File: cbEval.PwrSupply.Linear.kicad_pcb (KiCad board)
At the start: 2 copper layers, 35 x 109 mm, 38 parts, among them J1 CAL.CT3151V1-0, J10 Socket.Hor.2x5.6-5535512-4, J2 CAL.CT3151V1-2, J3 Keystone.4918, J4 Keystone.4918, J5 Keystone.3571, J6 Keystone.3571, J7 Socket.Hor.2x5.6-5535512-4, J8 Header.Hor.2x5.9-103326-0-05, J9 Header.Hor.2x5.9-103326-0-05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

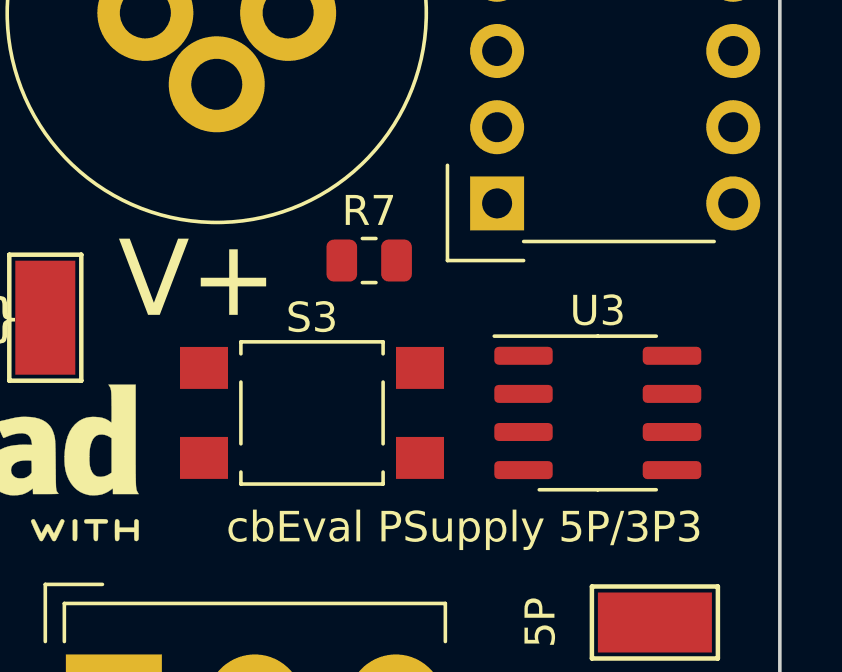
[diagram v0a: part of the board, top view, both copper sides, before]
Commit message: Bus-Leitungen neu belegt
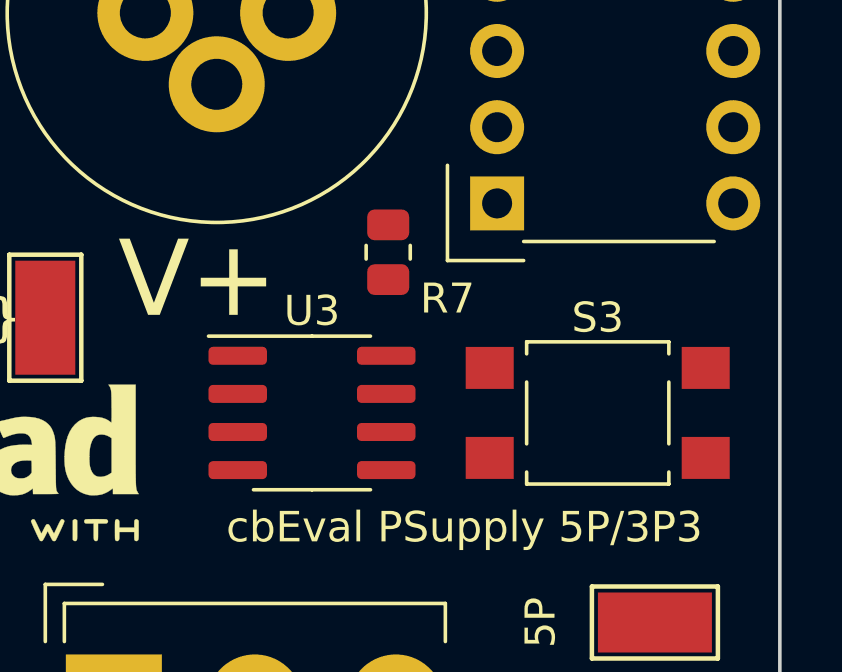
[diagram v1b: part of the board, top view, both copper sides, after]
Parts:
- moved S3 9.52 mm to (157.5, 77.5)
- moved U3 9.52 mm to (148.0, 77.5)
- moved R7 0.69 mm to (150.5, 72.1), turned to -90 degrees
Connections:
- J10 pad 10: /I2C-SCL -> /One-Wire
- J10 pad 9: /I2C-SDA -> /SPI-ADR2
- J7 pad 10: /PwrBus-Rsrvd1 -> /I2C-SCL
- J7 pad 9: /PwrBus-Rsrvd0 -> /I2C-SDA
- J8 pad 10: /PwrBus-Rsrvd1 -> /I2C-SCL
- J8 pad 9: /PwrBus-Rsrvd0 -> /I2C-SDA
- J9 pad 10: /I2C-SCL -> /One-Wire
- J9 pad 9: /I2C-SDA -> /SPI-ADR2
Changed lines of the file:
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@@
   (net 7 "Net-(D2-Pad4)")
   (net 8 "Net-(D1-Pad2)")
-  (net 9 "Net-(S2-Pad4)")
-  (net 10 "Net-(S2-Pad6)")
+  (net 9 "/SPI-ADR2")
+  (net 10 "/One-Wire")
   (net 11 "Net-(D2-Pad2)")
   (net 12 "+VDC")
@@
   (net 16 "unconnected-(S1-Pad4)")
   (net 17 "unconnected-(S1-Pad1)")
-  (net 18 "/PwrBus-Rsrvd1")
-  (net 19 "/PwrBus-Rsrvd0")
+  (net 18 "Net-(R5-Pad1)")
+  (net 19 "Net-(R6-Pad1)")
   (net 20 "~PWR-FAIL")
   (net 21 "-15V")
@@
       (net 5 "~RESET") (pinfunction "8") (pintype "passive"))
     (pad "9" thru_hole circle (at -7.87 -5.08) (size 1.8 1.8) (drill 1) (layers *.Cu *.Mask)
-      (net 19 "/PwrBus-Rsrvd0") (pinfunction "9") (pintype "passive"))
+      (net 24 "/I2C-SDA") (pinfunction "9") (pintype "passive"))
     (pad "10" thru_hole circle (at 0 -5.08) (size 1.8 1.8) (drill 1) (layers *.Cu *.Mask)
-      (net 18 "/PwrBus-Rsrvd1") (pinfunction "10") (pintype "passive"))
+      (net 23 "/I2C-SCL") (pinfunction "10") (pintype "passive"))
   )
   (footprint "BTech.Connector.4mm:CAL.CT3151V1" (layer "F.Cu")
@@
       (net 5 "~RESET") (pinfunction "8") (pintype "passive"))
     (pad "9" thru_hole oval (at 0 10.16 180) (locked) (size 1.7 1.7) (drill 1) (layers *.Cu *.Mask)
-      (net 19 "/PwrBus-Rsrvd0") (pinfunction "9") (pintype "passive"))
+      (net 24 "/I2C-SDA") (pinfunction "9") (pintype "passive"))
     (pad "10" thru_hole oval (at 2.54 10.16 180) (locked) (size 1.7 1.7) (drill 1) (layers *.Cu *.Mask)
-      (net 18 "/PwrBus-Rsrvd1") (pinfunction "10") (pintype "passive"))
+      (net 23 "/I2C-SCL") (pinfunction "10") (pintype "passive"))
     (model "${KICAD6_3DMODEL_DIR}/Connector_PinHeader_2.54mm.3dshapes/PinHeader_2x05_P2.54mm_Horizontal.wrl"
       (offset (xyz 0 0 0))
@@
     (fp_line (start 1 -0.625) (end 1 0.625) (layer "F.Fab") (width 0.1))
     (pad "1" smd roundrect (at -0.9125 0 90) (locked) (size 1.025 1.4) (layers "F.Cu" "F.Paste" "F.Mask") (roundrect_rratio 0.243902)
-      (net 8 "Net-(D1-Pad2)"))
+      (net 8 "Net-(D1-Pad2)") (pintype "passive"))
     (pad "2" smd roundrect (at 0.9125 0 90) (locked) (size 1.025 1.4) (layers "F.Cu" "F.Paste" "F.Mask") (roundrect_rratio 0.243902)
-      (net 3 "+5V"))
+      (net 3 "+5V") (pintype "passive"))
     (model "${KICAD6_3DMODEL_DIR}/Resistor_SMD.3dshapes/R_0805_2012Metric.wrl"
       (offset (xyz 0 0 0))
@@
       (net 4 "+3V3") (pinfunction "C") (pintype "passive"))
     (pad "4" thru_hole circle (at -4.7 2.415) (size 3.2 3.2) (drill 1.9) (layers *.Cu *.Mask)
-      (net 9 "Net-(S2-Pad4)") (pinfunction "A") (pintype "passive"))
+      (net 18 "Net-(R5-Pad1)") (pinfunction "A") (pintype "passive"))
     (pad "5" thru_hole circle (at 0 2.415) (size 3.2 3.2) (drill 1.9) (layers *.Cu *.Mask)
       (net 3 "+5V") (pinfunction "B") (pintype "passive"))
     (pad "6" thru_hole circle (at 4.7 2.415) (size 3.2 3.2) (drill 1.9) (layers *.Cu *.Mask)
-      (net 10 "Net-(S2-Pad6)") (pinfunction "C") (pintype "passive"))
+      (net 19 "Net-(R6-Pad1)") (pinfunction "C") (pintype "passive"))
   )
   (footprint "BTech.Connector.QuickConnect:Keystone.4918" (layer "F.Cu")
@@
     (fp_line (start 1 -0.625) (end 1 0.625) (layer "F.Fab") (width 0.1))
     (pad "1" smd roundrect (at -0.9125 0 270) (locked) (size 1.025 1.4) (layers "F.Cu" "F.Paste" "F.Mask") (roundrect_rratio 0.243902)
-      (net 10 "Net-(S2-Pad6)") (pintype "passive"))
+      (net 19 "Net-(R6-Pad1)") (pintype "passive"))
     (pad "2" smd roundrect (at 0.9125 0 270) (locked) (size 1.025 1.4) (layers "F.Cu" "F.Paste" "F.Mask") (roundrect_rratio 0.243902)
       (net 7 "Net-(D2-Pad4)") (pintype "passive"))
@@
   )
   (footprint "Package_SO:SOIC-8_3.9x4.9mm_P1.27mm" (layer "F.Cu")
-    (at 157.48 77.47)
+    (at 147.955 77.47)
     (descr "SOIC, 8 Pin (JEDEC MS-012AA, https://www.analog.com/media/en/package-pcb-resources/package/pkg_pdf/soic_narrow-r/r_8.pdf), generated with kicad-footprint-generator ipc_gullwing_generator.py")
     (tags "SOIC SO")
@@
       (net 25 "/SPI-ADR1") (pinfunction "8") (pintype "passive"))
     (pad "9" thru_hole oval (at 0 10.16 180) (locked) (size 1.7 1.7) (drill 1) (layers *.Cu *.Mask)
-      (net 24 "/I2C-SDA") (pinfunction "9") (pintype "passive"))
+      (net 9 "/SPI-ADR2") (pinfunction "9") (pintype "passive"))
     (pad "10" thru_hole oval (at 2.54 10.16 180) (locked) (size 1.7 1.7) (drill 1) (layers *.Cu *.Mask)
-      (net 23 "/I2C-SCL") (pinfunction "10") (pintype "passive"))
+      (net 10 "/One-Wire") (pinfunction "10") (pintype "passive"))
     (model "${KICAD6_3DMODEL_DIR}/Connector_PinHeader_2.54mm.3dshapes/PinHeader_2x05_P2.54mm_Horizontal.wrl"
       (offset (xyz 0 0 0))
@@
   )
   (footprint "Button_Switch_SMD:SW_SPST_TL3305A" (layer "F.Cu")
-    (at 147.955 77.47 180)
+    (at 157.48 77.47 180)
     (descr "https://www.e-switch.com/system/asset/product_line/data_sheet/213/TL3305.pdf")
     (tags "TL3305 Series Tact Switch")
@@
     (fp_line (start 1 0.625) (end -1 0.625) (layer "F.Fab") (width 0.1))
     (pad "1" smd roundrect (at -0.9125 0 90) (locked) (size 1.025 1.4) (layers "F.Cu" "F.Paste" "F.Mask") (roundrect_rratio 0.243902)
-      (net 9 "Net-(S2-Pad4)"))
+      (net 18 "Net-(R5-Pad1)") (pintype "passive"))
     (pad "2" smd roundrect (at 0.9125 0 90) (locked) (size 1.025 1.4) (layers "F.Cu" "F.Paste" "F.Mask") (roundrect_rratio 0.243902)
-      (net 6 "Net-(D1-Pad4)"))
+      (net 6 "Net-(D1-Pad4)") (pintype "passive"))
     (model "${KICAD6_3DMODEL_DIR}/Resistor_SMD.3dshapes/R_0805_2012Metric.wrl"
       (offset (xyz 0 0 0))
@@
       (net 25 "/SPI-ADR1") (pinfunction "8") (pintype "passive"))
     (pad "9" thru_hole circle (at -7.87 -5.08) (size 1.8 1.8) (drill 1) (layers *.Cu *.Mask)
-      (net 24 "/I2C-SDA") (pinfunction "9") (pintype "passive"))
+      (net 9 "/SPI-ADR2") (pinfunction "9") (pintype "passive"))
     (pad "10" thru_hole circle (at 0 -5.08) (size 1.8 1.8) (drill 1) (layers *.Cu *.Mask)
-      (net 23 "/I2C-SCL") (pinfunction "10") (pintype "passive"))
+      (net 10 "/One-Wire") (pinfunction "10") (pintype "passive"))
   )
   (footprint "LED_SMD:LED_Avago_PLCC4_3.2x2.8mm_CW" (layer "F.Cu")
@@
   )
   (footprint "Resistor_SMD:R_0805_2012Metric" (layer "F.Cu")
-    (at 149.86 72.39)
+    (at 150.495 72.1125 -90)
     (descr "Resistor SMD 0805 (2012 Metric), square (rectangular) end terminal, IPC_7351 nominal, (Body size source: IPC-SM-782 page 72, https://www.pcb-3d.com/wordpress/wp-content/uploads/ipc-sm-782a_amendment_1_and_2.pdf), generated with kicad-footprint-generator")
     (tags "resistor")
@@
     (property "Tolerance" "1%")
     (attr smd)
-    (fp_text reference "R7" (at 0 -1.65) (layer "F.SilkS")
+    (fp_text reference "R7" (at 1.5475 -1.9755 180) (layer "F.SilkS")
       (effects (font (size 1 1) (thickness 0.15)))
     )
-    (fp_text value "10k" (at 0 1.65) (layer "F.Fab") hide
+    (fp_text value "10k" (at 0 1.65 90) (layer "F.Fab") hide
       (effects (font (size 1 1) (thickness 0.15)))
     )
-    (fp_text user "${REFERENCE}" (at 0 0) (layer "F.Fab")
+    (fp_text user "${REFERENCE}" (at 0 0 90) (layer "F.Fab")
       (effects (font (size 0.5 0.5) (thickness 0.08)))
     )
@@
     (fp_line (start -1 0.625) (end -1 -0.625) (layer "F.Fab") (width 0.1))
     (fp_line (start -1 -0.625) (end 1 -0.625) (layer "F.Fab") (width 0.1))
-    (pad "1" smd roundrect (at -0.9125 0) (locked) (size 1.025 1.4) (layers "F.Cu" "F.Paste" "F.Mask") (roundrect_rratio 0.243902)
+    (pad "1" smd roundrect (at -0.9125 0 270) (locked) (size 1.025 1.4) (layers "F.Cu" "F.Paste" "F.Mask") (roundrect_rratio 0.243902)
       (net 1 "VCC") (pintype "passive"))
-    (pad "2" smd roundrect (at 0.9125 0) (locked) (size 1.025 1.4) (layers "F.Cu" "F.Paste" "F.Mask") (roundrect_rratio 0.243902)
+    (pad "2" smd roundrect (at 0.9125 0 270) (locked) (size 1.025 1.4) (layers "F.Cu" "F.Paste" "F.Mask") (roundrect_rratio 0.243902)
       (net 5 "~RESET") (pintype "passive"))
     (model "${KICAD6_3DMODEL_DIR}/Resistor_SMD.3dshapes/R_0805_2012Metric.wrl"

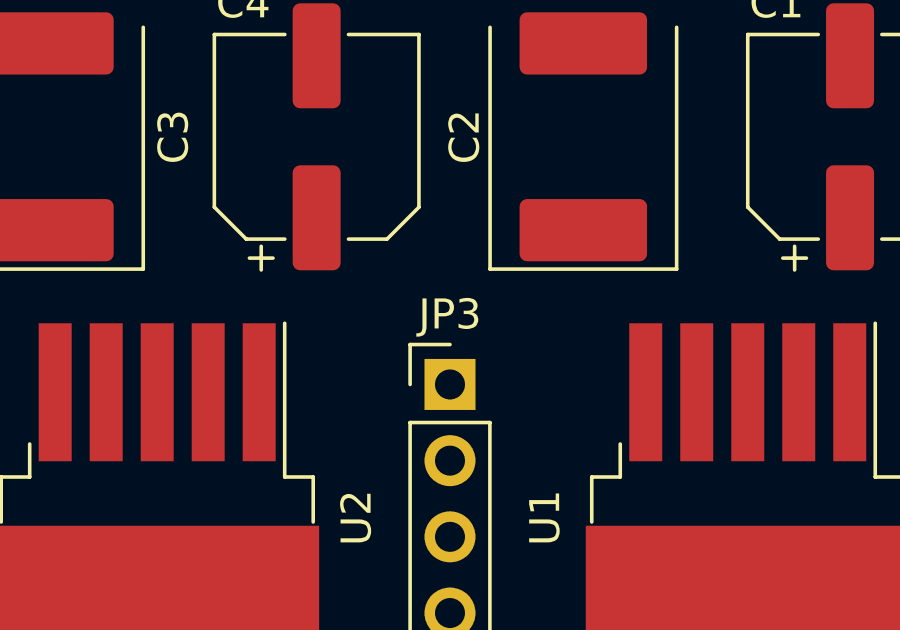
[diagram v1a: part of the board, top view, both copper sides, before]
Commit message: Bauteil (PinHeader) ausgetauscht
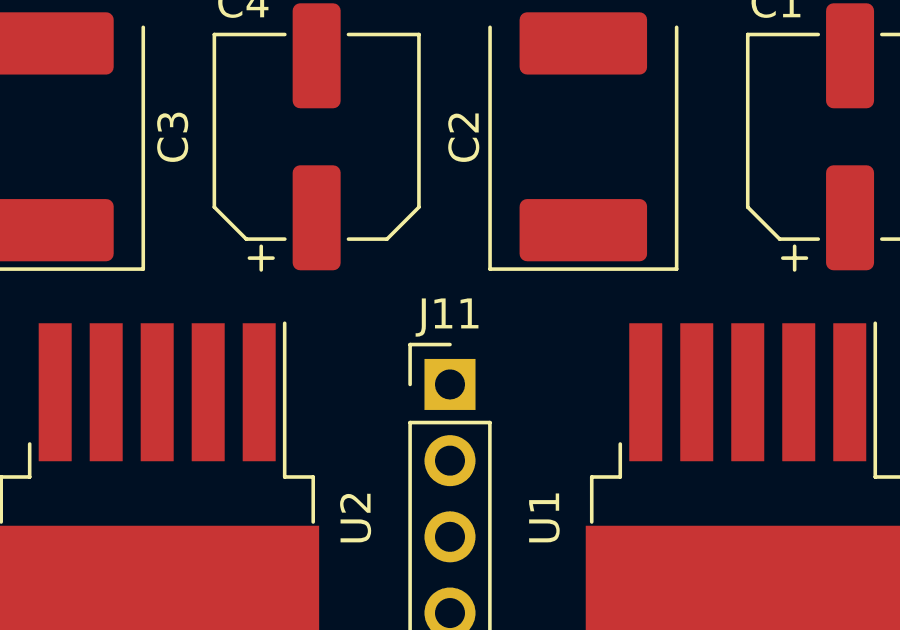
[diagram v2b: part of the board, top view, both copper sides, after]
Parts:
- renumbered JP3 to J11
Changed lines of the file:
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@@
     (property "Usage" "GND")
     (attr through_hole)
-    (fp_text reference "JP3" (at 0 -2.33) (layer "F.SilkS")
+    (fp_text reference "J11" (at 0 -2.33) (layer "F.SilkS")
       (effects (font (size 1 1) (thickness 0.15)))
     )

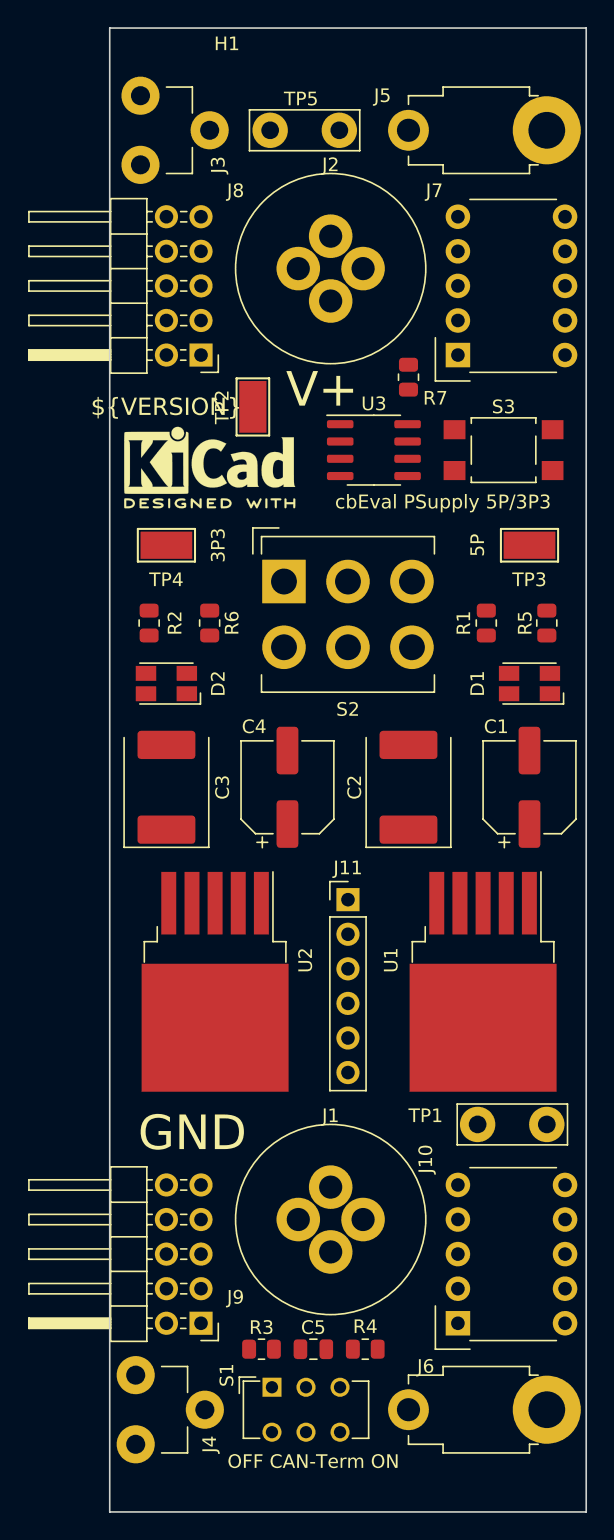
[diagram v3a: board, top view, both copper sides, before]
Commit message: Bus-Stecker getauscht
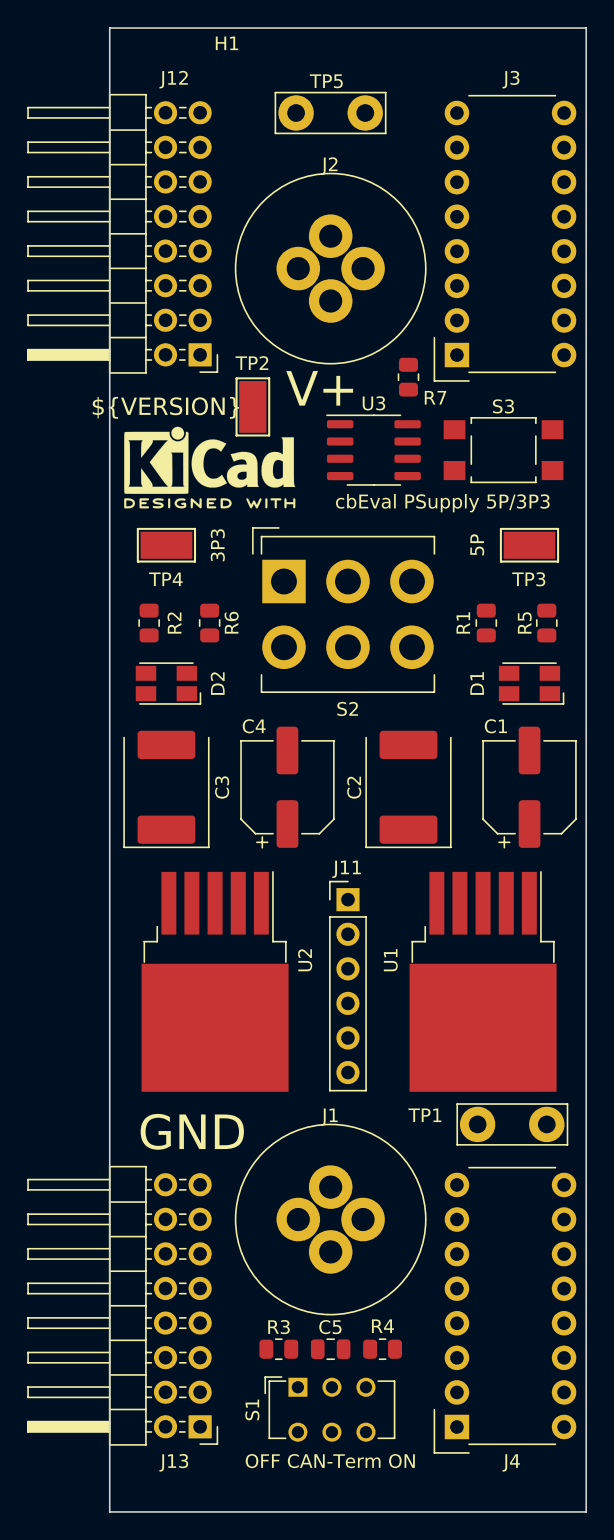
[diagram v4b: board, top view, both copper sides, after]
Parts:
- removed J10, J7: Socket.Hor.2x5.6-5535512-4, BTech.Connector.AMPMODU-ModII:Socket.Hor.2x5.6-5535512-4
- removed J5, J6: Keystone.3571, BTech.Connector.QuickConnect:Keystone.3571
- removed J8, J9: Header.Hor.2x5.9-103326-0-05, Connector_PinHeader_2.54mm:PinHeader_2x05_P2.54mm_Horizontal
- added J12: Header.Hor.2x8.9-103326-0-08, Connector_PinHeader_2.54mm:PinHeader_2x08_P2.54mm_Horizontal, F.Cu at (135.2, 70.5)
- added J13: Header.Hor.2x8.9-103326-0-08, Connector_PinHeader_2.54mm:PinHeader_2x08_P2.54mm_Horizontal, F.Cu at (135.2, 149.2)
- J3, J4: value Keystone.4918 -> Socket.Hor.2x8.1-5535512-8; footprint BTech.Connector.QuickConnect:Keystone.4918 -> BTech.Connector.AMPMODU-ModII:Socket.Hor.2x5.6-5535512-4
- moved J3 32.4 mm to (161.9, 62.9)
- moved J4 32.1 mm to (161.9, 141.6)
- moved TP5 2.29 mm to (147.3, 52.7)
- moved S1 1.91 mm to (142.4, 146.3)
- moved C5 1.27 mm to (144.8, 143.5)
- moved R3 1.27 mm to (141.0, 143.5)
- moved R4 1.27 mm to (148.6, 143.5)
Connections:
- J3 pad 1: GND -> VCC

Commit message: Properties geändert, Logo aktualisiert
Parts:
- MP1: value KiCAD-Logo2.5mm.SilkScreen -> KiCAD-DesignedWith-Logo2.5mm.SilkScreen

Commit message: Layout fertig
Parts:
- moved R7 1.11 mm to (149.9, 73.0), turned to 0 degrees
- turned R5 to -90 degrees
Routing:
- net +3V3: track 0.00 -> 141.2 mm, vias 0 -> 4
- net +VDC: track 0.00 -> 123.4 mm, vias 0 -> 2
- net +5V: track 0.00 -> 98.3 mm, vias 0 -> 3
- net ~PWR-FAIL: track 0.00 -> 72.8 mm, vias 0 -> 5
- net /Reserved1: track 0.00 -> 60.7 mm
- net ~RESET: track 0.00 -> 57.4 mm, vias 0 -> 1
- net VCC: track 0.00 -> 49.2 mm, vias 0 -> 2
- net /SPI-ADR1: track 0.00 -> 33.5 mm
- net /SPI-MRST: track 0.00 -> 33.2 mm
- net -15V: track 0.00 -> 33.2 mm
- net /One-Wire: track 0.00 -> 33.0 mm
- net /SPI-~CE: track 0.00 -> 32.4 mm
- net /CAN-L: track 0.00 -> 31.7 mm
- net /I2C-SCL: track 0.00 -> 30.8 mm
- net Net-(R5-Pad1): track 0.00 -> 24.1 mm, vias 0 -> 1
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- added copper zone on B.Cu, net GND
- added copper zone on F.Cu, net GND
